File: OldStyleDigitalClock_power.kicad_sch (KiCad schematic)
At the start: 14 parts, among them J1 USB_C_IN, J2 USB_A_OUT, J3 USB_A_OUT

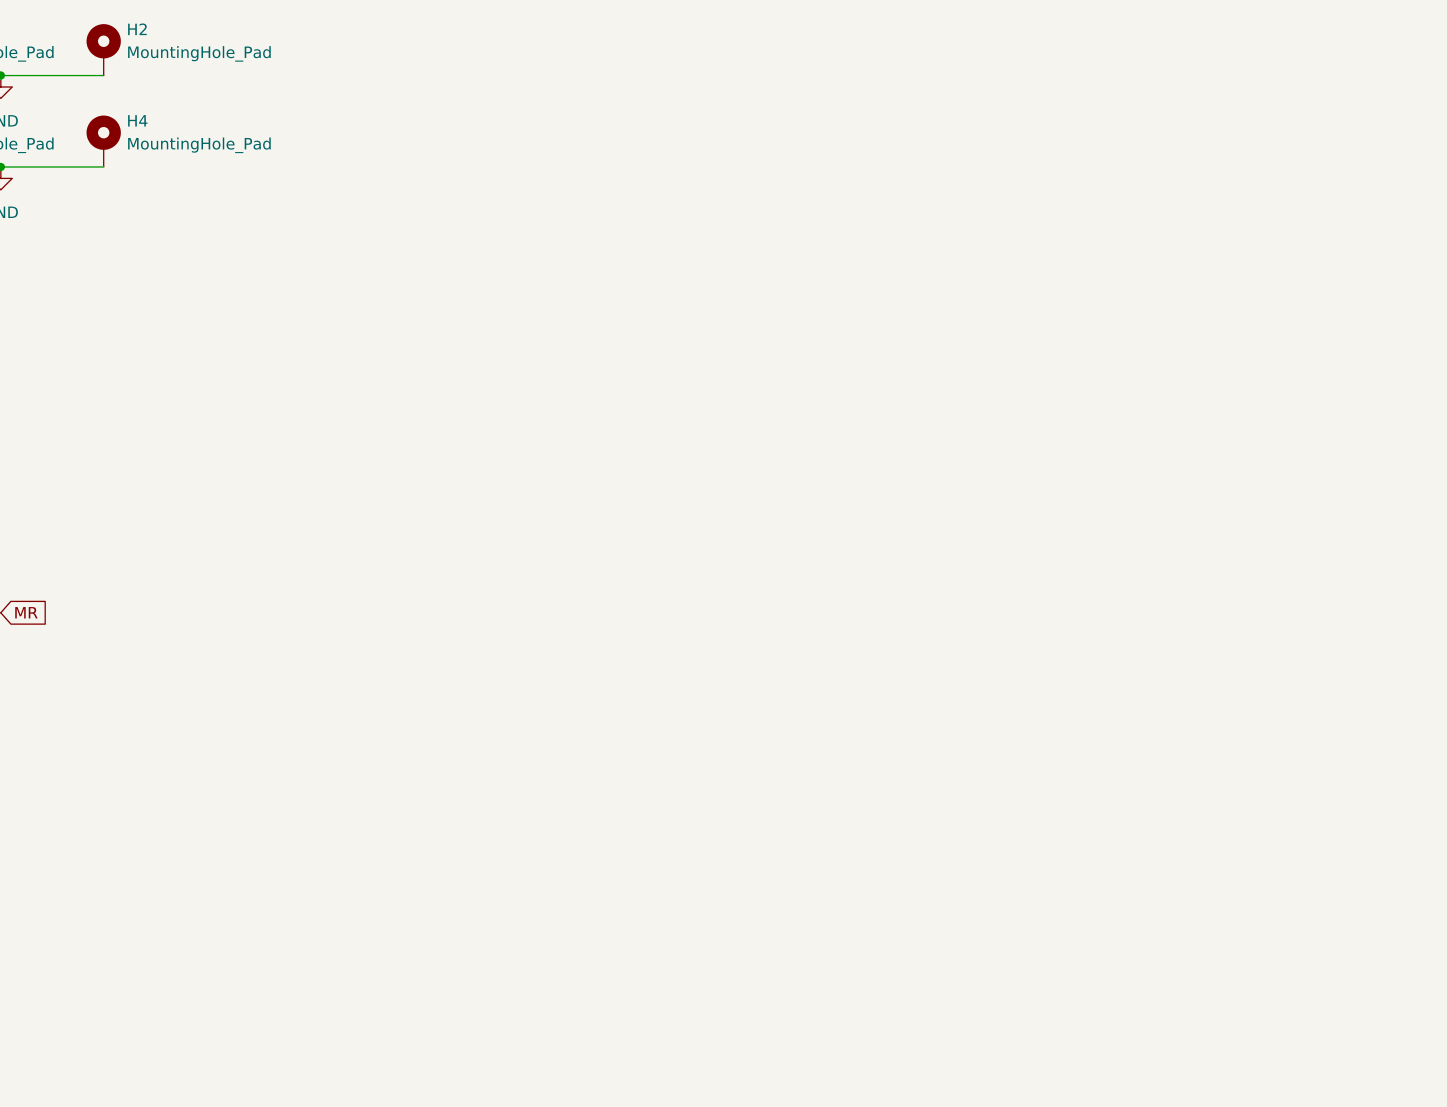
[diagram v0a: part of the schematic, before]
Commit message: Using standard astable multivibrator for LED dimming
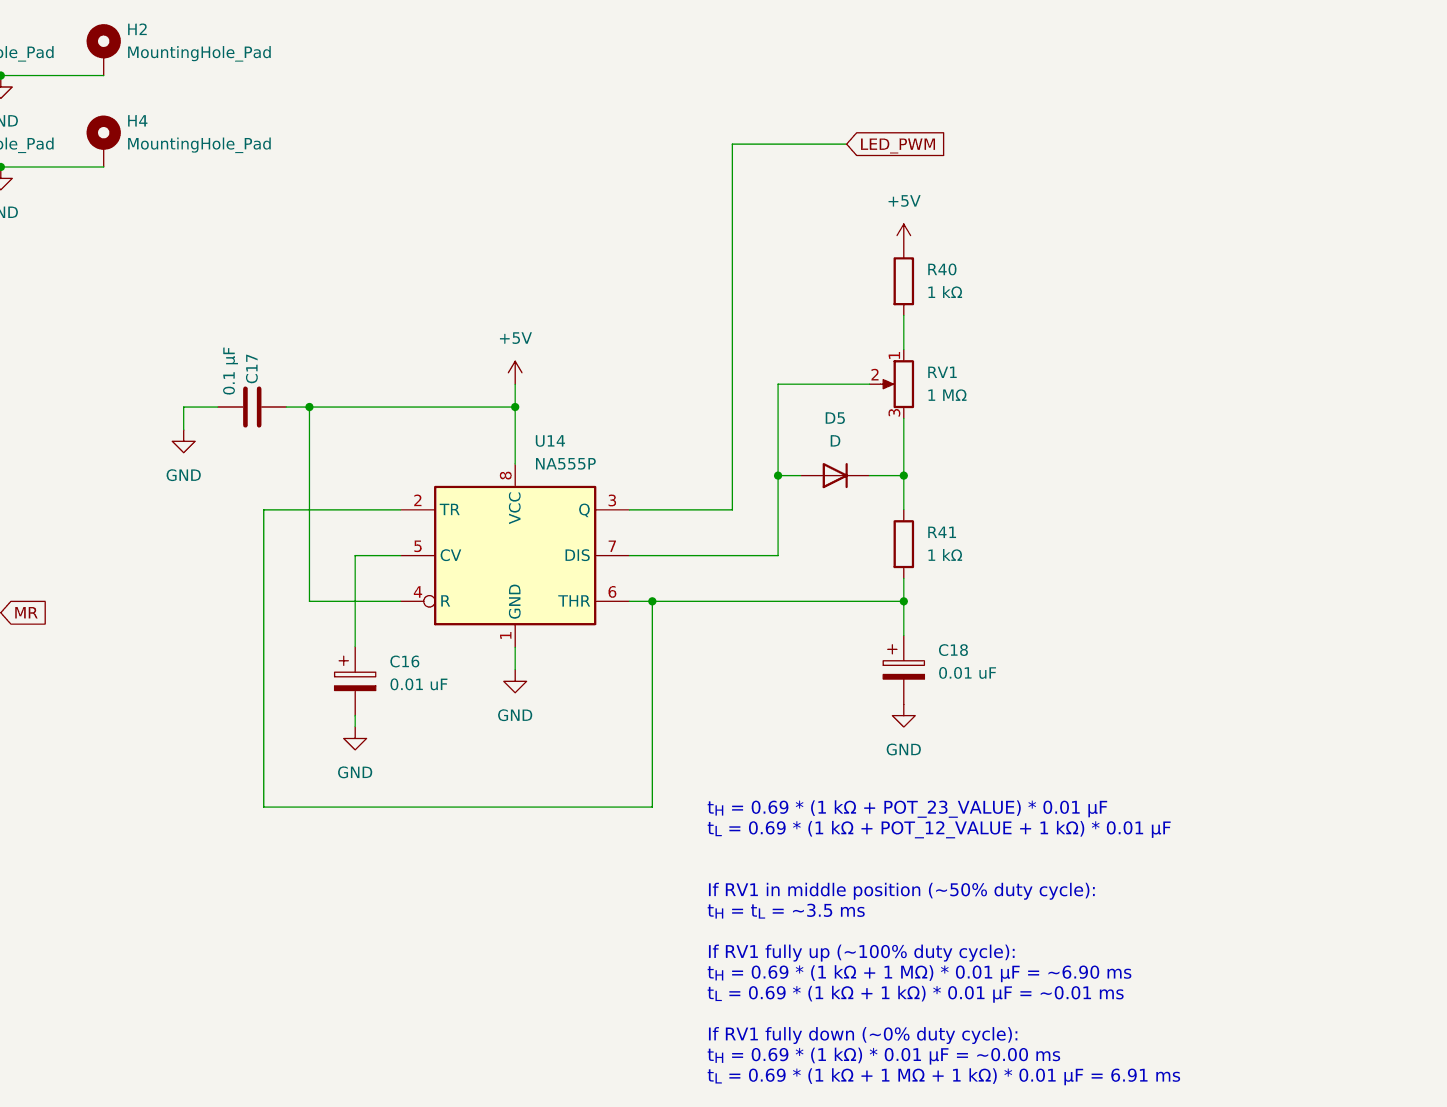
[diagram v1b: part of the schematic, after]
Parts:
- added C16, C18: 0.01 uF, symbol Device:C_Polarized
- added C17: 0.1 µF, Capacitor_THT:C_Disc_D5.1mm_W3.2mm_P5.00mm, symbol Device:C
- added D5: D, symbol Device:D
- added R40, R41: 1 kΩ, symbol Device:R
- added RV1: 1 MΩ, symbol Device:R_Potentiometer
- added U14: NA555P, Package_DIP:DIP-8_W7.62mm, symbol Timer:NA555P
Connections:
- net +5V: now also C17.1, R40.1, U14.4 (R), U14.8 (VCC)
- net GND: now also C16.2, C17.2, C18.2, U14.1 (GND)
- new net: D5.1 (K), R41.1, RV1.3
- new net: D5.2 (A), RV1.2, U14.7 (DIS)
- new net: C18.1, R41.2, U14.2 (TR), U14.6 (THR)
- new net: R40.2, RV1.1
- new net: C16.1, U14.5 (CV)
- new net LED_PWM: U14.3 (Q)
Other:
- note added: "t_{H} = 0.69 * (1 kΩ + POT_23_VALUE) * 0.01 µF t_{L} = 0.69 * (1 kΩ + POT_12_VALUE + 1 kΩ) * 0.01 µF If RV1 in middle position (~50% duty cycle): t_{H} = t_{L} = ~3.5 ms If RV1 fully up (~100% duty cycle): t_{H} = 0.69 * (1 kΩ + 1 MΩ) * 0.01 µF = ~6.90 ms t_{L} = 0.69 * (1 kΩ + 1 kΩ) * 0.01 µF = ~0.01 ms If RV1 fully down (~0% duty cycle): t_{H} = 0.69 * (1 kΩ) * 0.01 µF = ~0.00 ms t_{L} = 0.69 *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"
- company: (none) -> Pasquale Lafiosca
- title: (none) -> Old style digital clock

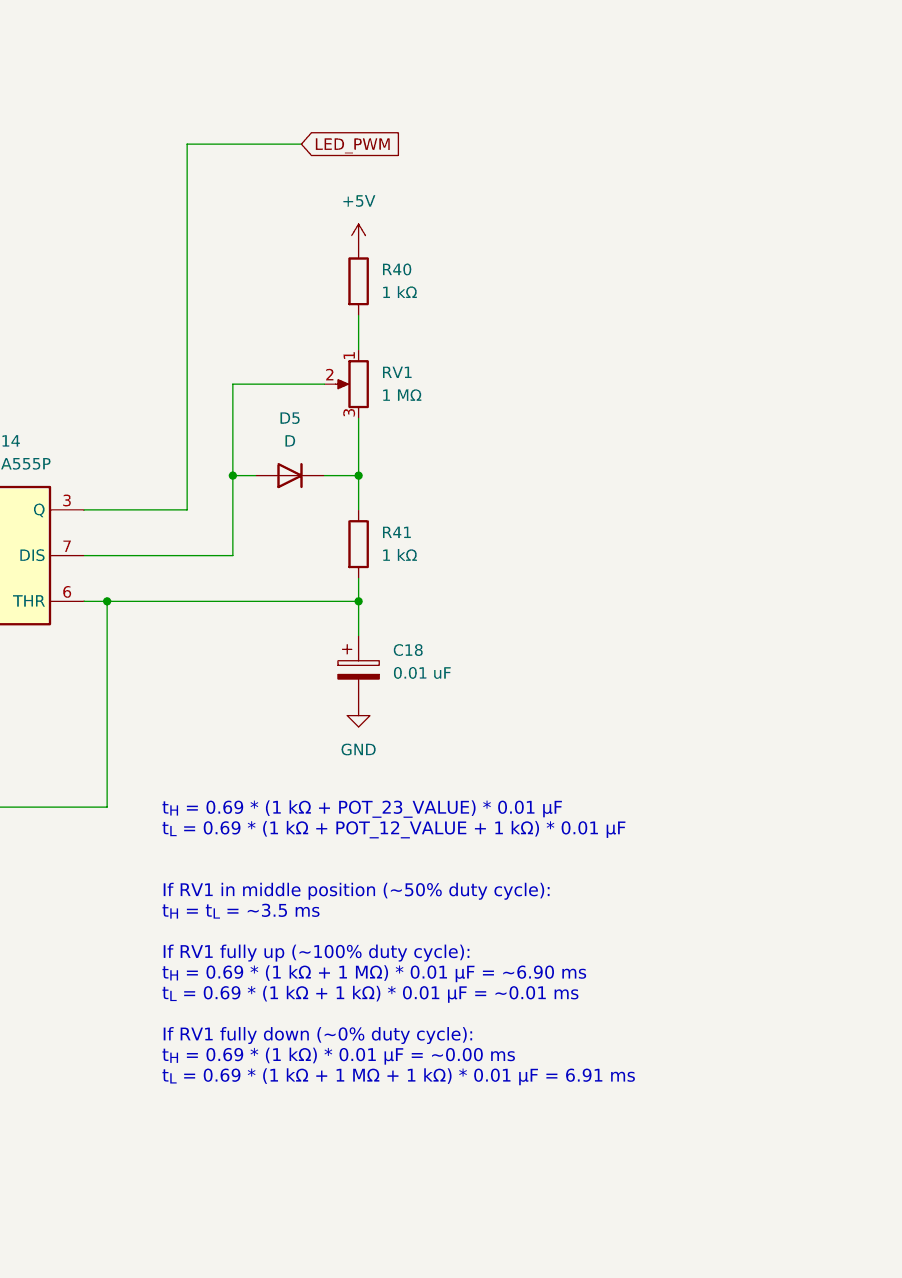
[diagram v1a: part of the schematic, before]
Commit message: Added photoresistor for automatic brightness adjustment
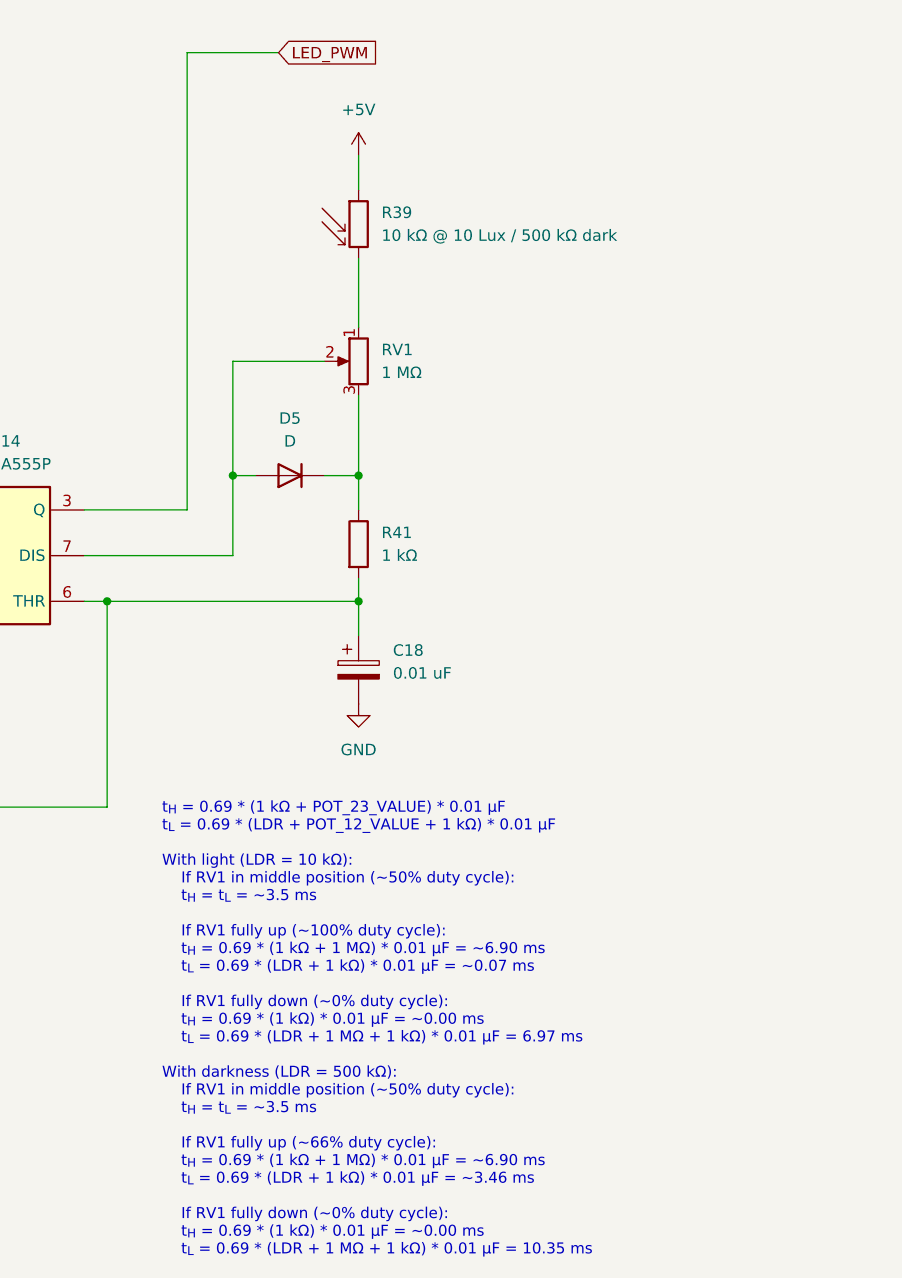
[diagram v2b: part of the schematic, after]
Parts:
- removed R40: 1 kΩ, symbol Device:R
- added R39: 10 kΩ @ 10 Lux / 500 kΩ dark, symbol Device:R_Photo
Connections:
- net +5V: now also R39.1
- net at RV1.1: now also R39.2
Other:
- note added: "t_{H} = 0.69 * (1 kΩ + POT_23_VALUE) * 0.01 µF t_{L} = 0.69 * (LDR + POT_12_VALUE + 1 kΩ) * 0.01 µF With light (LDR = 10 kΩ): If RV1 in middle position (~50% duty cycle): t_{H} = t_{L} = ~3.5 ms If RV1 fully up (~100% duty cycle): t_{H} = 0.69 * (1 kΩ + 1 MΩ) * 0.01 µF = ~6.90 ms t_{L} = 0.69 * (LDR + 1 kΩ) * 0.01 µF = ~0.07 ms If RV1 fully down (~0% duty cycle): t_{H} = 0.69 * (1 kΩ) * 0.01 µF =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"
- note removed: "t_{H} = 0.69 * (1 kΩ + POT_23_VALUE) * 0.01 µF t_{L} = 0.69 * (1 kΩ + POT_12_VALUE + 1 kΩ) * 0.01 µF If RV1 in middle position (~50% duty cycle): t_{H} = t_{L} = ~3.5 ms If RV1 fully up (~100% duty cycle): t_{H} = 0.69 * (1 kΩ + 1 MΩ) * 0.01 µF = ~6.90 ms t_{L} = 0.69 * (1 kΩ + 1 kΩ) * 0.01 µF = ~0.01 ms If RV1 fully down (~0% duty cycle): t_{H} = 0.69 * (1 kΩ) * 0.01 µF = ~0.00 ms t_{L} = 0.69 *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"
- moved on the sheet: RV1
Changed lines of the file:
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@@
 		(company "Pasquale Lafiosca")
 	)
-	(text "t_{H} = 0.69 * (1 kΩ + POT_23_VALUE) * 0.01 µF\nt_{L} = 0.69 * (1 kΩ + POT_12_VALUE + 1 kΩ) * 0.01 µF\n\n\nIf RV1 in middle position (~50% duty cycle):\nt_{H} = t_{L} = ~3.5 ms\n\nIf RV1 fully up (~100% duty cycle):\nt_{H} = 0.69 * (1 kΩ + 1 MΩ) * 0.01 µF = ~6.90 ms\nt_{L} = 0.69 * (1 kΩ + 1 kΩ) * 0.01 µF = ~0.01 ms\n\nIf RV1 fully down (~0% duty cycle):\nt_{H} = 0.69 * (1 kΩ) * 0.01 µF = ~0.00 ms\nt_{L} = 0.69 * (1 kΩ + 1 MΩ + 1 kΩ) * 0.01 µF = 6.91 ms"
+	(text "t_{H} = 0.69 * (1 kΩ + POT_23_VALUE) * 0.01 µF\nt_{L} = 0.69 * (LDR + POT_12_VALUE + 1 kΩ) * 0.01 µF\n\nWith light (LDR = 10 kΩ):\n	If RV1 in middle position (~50% duty cycle):\n	t_{H} = t_{L} = ~3.5 ms\n\n	If RV1 fully up (~100% duty cycle):\n	t_{H} = 0.69 * (1 kΩ + 1 MΩ) * 0.01 µF = ~6.90 ms\n	t_{L} = 0.69 * (LDR + 1 kΩ) * 0.01 µF = ~0.07 ms\n\n	If RV1 fully down (~0% duty cycle):\n	t_{H} = 0.69 * (1 kΩ) * 0.01 µF = ~0.00 ms\n	t_{L} = 0.69 * (LDR + 1 MΩ + 1 kΩ) * 0.01 µF = 6.97 ms\n\nWith darkness (LDR = 500 kΩ):\n	If RV1 in middle position (~50% duty cycle):\n	t_{H} = t_{L} = ~3.5 ms\n\n	If RV1 fully up (~66% duty cycle):\n	t_{H} = 0.69 * (1 kΩ + 1 MΩ) * 0.01 µF = ~6.90 ms\n	t_{L} = 0.69 * (LDR + 1 kΩ) * 0.01 µF = ~3.46 ms\n\n	If RV1 fully down (~0% duty cycle):\n	t_{H} = 0.69 * (1 kΩ) * 0.01 µF = ~0.00 ms\n	t_{L} = 0.69 * (LDR + 1 MΩ + 1 kΩ) * 0.01 µF = 10.35 ms"
 		(exclude_from_sim no)
 		(at 211.836 111.252 0)
 		(effects
 			(font
-				(size 1.4224 1.4224)
+				(size 1.2192 1.2192)
 			)
 			(justify left top)
@@
 	(wire
 		(pts
+			(xy 233.68 39.37) (xy 233.68 43.18)
+		)
+		(stroke
+			(width 0)
+			(type default)
+		)
+	)
+	(wire
+		(pts
 			(xy 88.9 69.85) (xy 88.9 80.01)
 		)
@@
 	(wire
 		(pts
-			(xy 233.68 74.93) (xy 233.68 68.58)
-		)
-		(stroke
-			(width 0)
-			(type default)
-		)
-	)
-	(wire
-		(pts
 			(xy 219.71 83.82) (xy 203.2 83.82)
 		)
@@
 	(wire
 		(pts
-			(xy 214.63 38.1) (xy 227.33 38.1)
+			(xy 214.63 27.94) (xy 224.79 27.94)
 		)
 		(stroke
@@
 	(wire
 		(pts
-			(xy 219.71 64.77) (xy 229.87 64.77)
+			(xy 219.71 62.23) (xy 229.87 62.23)
 		)
 		(stroke
@@
 	(wire
 		(pts
-			(xy 214.63 38.1) (xy 214.63 78.74)
+			(xy 214.63 27.94) (xy 214.63 78.74)
 		)
 		(stroke
@@
 	(wire
 		(pts
-			(xy 219.71 64.77) (xy 219.71 74.93)
+			(xy 219.71 62.23) (xy 219.71 74.93)
 		)
 		(stroke
@@
 	(wire
 		(pts
-			(xy 233.68 57.15) (xy 233.68 60.96)
-		)
-		(stroke
-			(width 0)
-			(type default)
-		)
-	)
-	(wire
-		(pts
 			(xy 153.67 67.31) (xy 153.67 69.85)
 		)
@@
 	(wire
 		(pts
+			(xy 233.68 66.04) (xy 233.68 74.93)
+		)
+		(stroke
+			(width 0)
+			(type default)
+		)
+	)
+	(wire
+		(pts
 			(xy 162.56 111.76) (xy 205.74 111.76)
 		)
@@
 		(pts
 			(xy 115.57 85.09) (xy 115.57 90.17)
+		)
+		(stroke
+			(width 0)
+			(type default)
+		)
+	)
+	(wire
+		(pts
+			(xy 233.68 50.8) (xy 233.68 58.42)
 		)
 		(stroke
@@
 	(global_label "LED_PWM"
 		(shape input)
-		(at 227.33 38.1 0)
+		(at 224.79 27.94 0)
 		(fields_autoplaced yes)
 		(effects
@@
 		)
 		(property "Intersheetrefs" "${INTERSHEET_REFS}"
-			(at 238.9027 38.1 0)
+			(at 236.3627 27.94 0)
 			(effects
 				(font
@@
 	(symbol
 		(lib_id "Device:R_Potentiometer")
-		(at 233.68 64.77 0)
+		(at 233.68 62.23 0)
 		(mirror y)
 		(unit 1)
@@
 		(dnp no)
 		(property "Reference" "RV1"
+			(at 236.22 60.9599 0)
+			(effects
+				(font
+					(size 1.27 1.27)
+				)
+				(justify right)
+			)
+		)
+		(property "Value" "1 MΩ"
 			(at 236.22 63.4999 0)
 			(effects
@@
 			)
 		)
-		(property "Value" "1 MΩ"
-			(at 236.22 66.0399 0)
-			(effects
-				(font
-					(size 1.27 1.27)
-				)
-				(justify right)
-			)
-		)
 		(property "Footprint" ""
-			(at 233.68 64.77 0)
+			(at 233.68 62.23 0)
 			(effects
 				(font
@@
 		)
 		(property "Datasheet" "~"
-			(at 233.68 64.77 0)
+			(at 233.68 62.23 0)
 			(effects
 				(font
@@
 		)
 		(property "Description" "Potentiometer"
-			(at 233.68 64.77 0)
+			(at 233.68 62.23 0)
 			(effects
 				(font
@@
 	(symbol
 		(lib_id "power:VDD")
-		(at 233.68 49.53 0)
+		(at 233.68 39.37 0)
 		(unit 1)
 		(exclude_from_sim no)
@@
 		(dnp no)
 		(property "Reference" "#PWR063"
-			(at 233.68 53.34 0)
+			(at 233.68 43.18 0)
 			(effects
 				(font
@@
 		)
 		(property "Value" "+5V"
-			(at 233.68 44.45 0)
+			(at 233.68 34.29 0)
 			(effects
 				(font
@@
 		)
 		(property "Footprint" ""
-			(at 233.68 49.53 0)
+			(at 233.68 39.37 0)
 			(effects
 				(font
@@
 		)
 		(property "Datasheet" ""
-			(at 233.68 49.53 0)
+			(at 233.68 39.37 0)
 			(effects
 				(font
@@
 		)
 		(property "Description" ""
-			(at 233.68 49.53 0)
+			(at 233.68 39.37 0)
 			(effects
 				(font
@@
 				(path "/a24f1d5b-eb61-47a3-9a92-6515e74f7a21/31b03831-3d01-49ef-8f86-173fa6c5d953"
 					(reference "#PWR063")
-					(unit 1)
-				)
-			)
-		)
-	)
-	(symbol
-		(lib_id "Device:R")
-		(at 233.68 53.34 0)
-		(unit 1)
-		(exclude_from_sim no)
-		(in_bom yes)
-		(on_board yes)
-		(dnp no)
-		(fields_autoplaced yes)
-		(property "Reference" "R40"
-			(at 236.22 52.0699 0)
-			(effects
-				(font
-					(size 1.27 1.27)
-				)
-				(justify left)
-			)
-		)
-		(property "Value" "1 kΩ"
-			(at 236.22 54.6099 0)
-			(effects
-				(font
-					(size 1.27 1.27)
-				)
-				(justify left)
-			)
-		)
-		(property "Footprint" ""
-			(at 231.902 53.34 90)
-			(effects
-				(font
-					(size 1.27 1.27)
-				)
-				(hide yes)
-			)
-		)
-		(property "Datasheet" "~"
-			(at 233.68 53.34 0)
-			(effects
-				(font
-					(size 1.27 1.27)
-				)
-				(hide yes)
-			)
-		)
-		(property "Description" "Resistor"
-			(at 233.68 53.34 0)
-			(effects
-				(font
-					(size 1.27 1.27)
-				)
-				(hide yes)
-			)
-		)
-		(pin "2"
-		)
-		(pin "1"
-		)
-		(instances
-			(project ""
-				(path "/a24f1d5b-eb61-47a3-9a92-6515e74f7a21/31b03831-3d01-49ef-8f86-173fa6c5d953"
-					(reference "R40")
 					(unit 1)
 				)
@@
 					(unit 1)
 				)
+			)
+		)
+	)
+	(symbol
+		(lib_id "Device:R_Photo")
+		(at 233.68 46.99 0)
+		(unit 1)
+		(exclude_from_sim no)
+		(in_bom yes)
+		(on_board yes)
+		(dnp no)
+		(fields_autoplaced yes)
+		(property "Reference" "R39"
+			(at 236.22 45.7199 0)
+			(effects
+				(font
+					(size 1.27 1.27)
+				)
+				(justify left)
+			)
+		)
+		(property "Value" "10 kΩ @ 10 Lux / 500 kΩ dark"
+			(at 236.22 48.2599 0)
+			(effects
+				(font
+					(size 1.27 1.27)
+				)
+				(justify left)
+			)
+		)
+		(property "Footprint" ""
+			(at 234.95 53.34 90)
+			(effects
+				(font
+					(size 1.27 1.27)
+				)
+				(justify left)
+				(hide yes)
+			)
+		)
+		(property "Datasheet" "~"
+			(at 233.68 48.26 0)
+			(effects
+				(font
+					(size 1.27 1.27)
+				)
+				(hide yes)
+			)
+		)
+		(property "Description" "Photoresistor"
+			(at 233.68 46.99 0)
+			(effects
+				(font
+					(size 1.27 1.27)
+				)
+				(hide yes)
+			)
+		)
+		(pin "2"
+		)
+		(pin "1"
+		)
+		(instances
+			(project ""
+				(path "/a24f1d5b-eb61-47a3-9a92-6515e74f7a21/31b03831-3d01-49ef-8f86-173fa6c5d953"
+					(reference "R39")
+					(unit 1)
+				)
